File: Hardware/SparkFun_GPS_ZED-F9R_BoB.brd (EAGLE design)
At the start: 43.2 x 50.8 mm, 147 parts, among them J1 U.FL, J3 QWIIC_RIGHT_ANGLE, J4 QWIIC_RIGHT_ANGLE, U1 UBLOX_ZED_F9R, U2 3.3V, U4 HCPL-270L

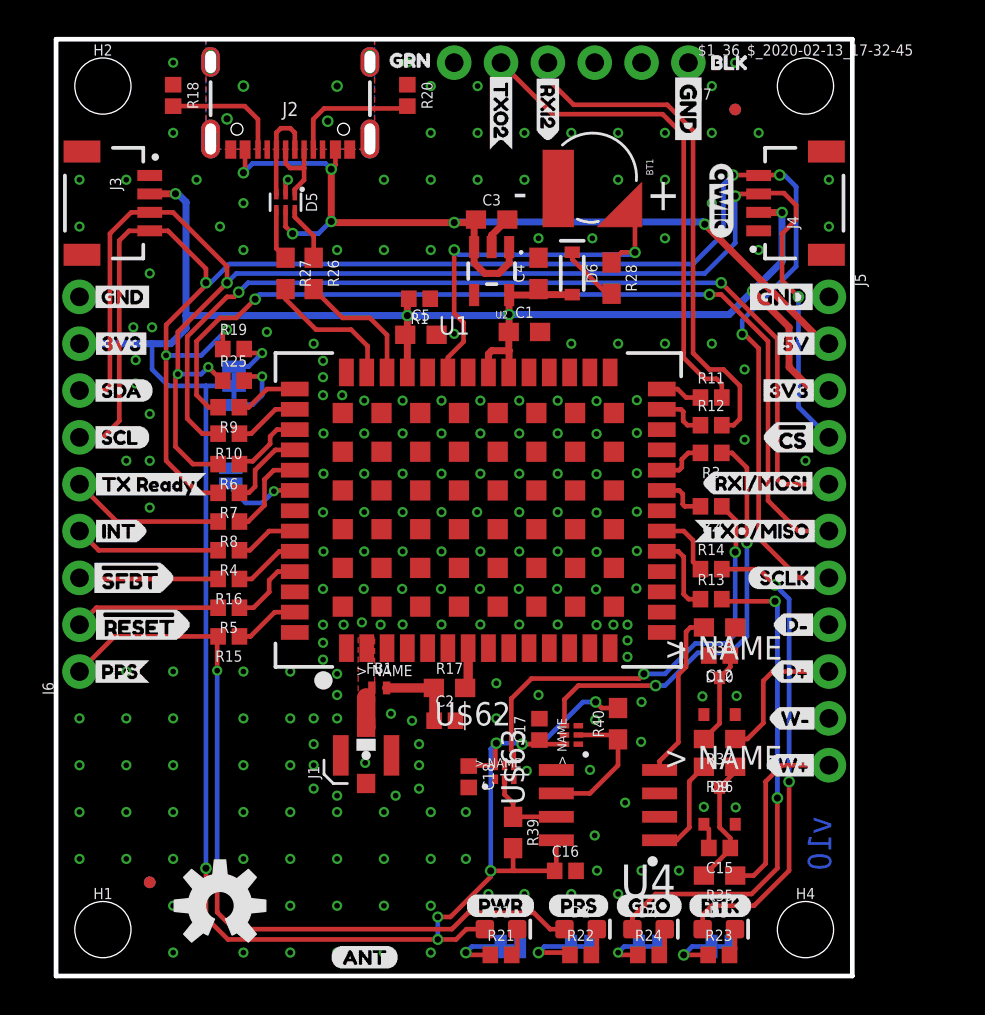
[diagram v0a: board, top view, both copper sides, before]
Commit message: Renumbers parts, updates parts with PROD_IDs that didn't have them before
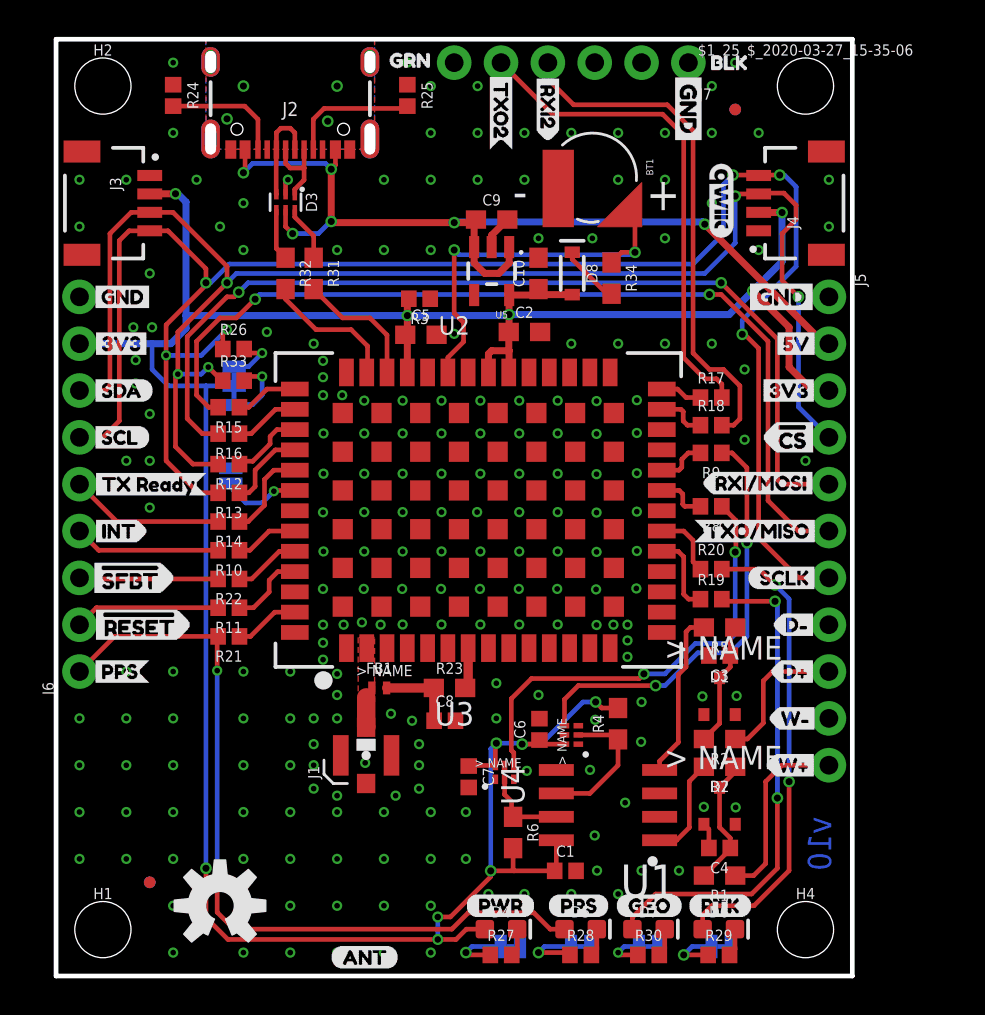
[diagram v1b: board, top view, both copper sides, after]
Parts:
- removed C12, C15: 1nF, SparkFun-Capacitors:0402
- removed C16: 0.1uF, SparkFun-Capacitors:0402
- removed D10, D9: 0.5A/40V/420mV, classified:SOT23_BZX
- removed R35, R37: 3.3k, SparkFun-Resistors:0603
- removed R36, R38: 470, SparkFun-Resistors:0603
- removed R39, R40: 910, classified:0603
- removed U$63: UHS_INVERTER_SCHMITT_TRIGGERSIP6, classified:SIP6
- added C10, C9: 1.0uF, SparkFun-Capacitors:0603
- added C8: 47pF, SparkFun-Capacitors:0402
- added D7: BLUE, SparkFun-LED:LED-0603
- added D8: 0.5A/40V/420mV, SparkFun-DiscreteSemi:SOD-323
- added R29, R30: 1KOHM-0402-1/16W-1%, SparkFun-Resistors:0402
- added R31, R32: 27, SparkFun-Resistors:0603
- added R33: 2.2K, SparkFun-Resistors:0402
- added R34: 3.3k, SparkFun-Resistors:0603
- added U5: 3.3V, SparkFun-IC-Power:SOT23-5
- C1: value 1.0uF -> 0.1uF; device SparkFun-Capacitors:0603 -> SparkFun-Capacitors:0402
- C2: value 47pF -> 1.0uF; device SparkFun-Capacitors:0402 -> SparkFun-Capacitors:0603
- C3, C4: value 1.0uF -> 1nF; device SparkFun-Capacitors:0603 -> SparkFun-Capacitors:0402
- D1: value RED -> 0.5A/40V/420mV; device SparkFun-LED:LED-0603 -> classified:SOT23_BZX
- D2: value BLUE -> 0.5A/40V/420mV; device SparkFun-LED:LED-0603 -> classified:SOT23_BZX
- D3: value BLUE -> PRTR5V0U2F; device SparkFun-LED:LED-0603 -> SparkFun-IC-Power:SOT886
- D4: value BLUE -> RED
- D5: value PRTR5V0U2F -> BLUE; device SparkFun-IC-Power:SOT886 -> SparkFun-LED:LED-0603
- D6: value 0.5A/40V/420mV -> BLUE; device SparkFun-DiscreteSemi:SOD-323 -> SparkFun-LED:LED-0603
- R1: value 100K -> 3.3k; device SparkFun-Resistors:0402 -> SparkFun-Resistors:0603
- R17: device SparkFun-Resistors:0603 -> SparkFun-Resistors:0402
- R18, R20: value 5.1k -> 33
- R19: value 2.2K -> 33
- R2: value 33 -> 3.3k; device SparkFun-Resistors:0402 -> SparkFun-Resistors:0603
- R21, R22: value 1KOHM-0402-1/16W-1% -> 33
- R23: value 1KOHM-0402-1/16W-1% -> 33; device SparkFun-Resistors:0402 -> SparkFun-Resistors:0603
- R24: value 1KOHM-0402-1/16W-1% -> 5.1k
- R25: value 2.2K -> 5.1k
- R26: value 27 -> 2.2K; device SparkFun-Resistors:0603 -> SparkFun-Resistors:0402
- R27: value 27 -> 1KOHM-0402-1/16W-1%; device SparkFun-Resistors:0603 -> SparkFun-Resistors:0402
- R28: value 3.3k -> 1KOHM-0402-1/16W-1%; device SparkFun-Resistors:0603 -> SparkFun-Resistors:0402
- R3: value 33 -> 100K
- R4, R6: value 33 -> 910; device SparkFun-Resistors:0402 -> classified:0603
- R5, R7: value 33 -> 470; device SparkFun-Resistors:0402 -> SparkFun-Resistors:0603
- U1: value UBLOX_ZED_F9R -> HCPL-073L; device classified:UBLOX_ZED_F9R -> classified:SOP_8-PIN
- U2: value 3.3V -> UBLOX_ZED_F9R; device SparkFun-IC-Power:SOT23-5 -> classified:UBLOX_ZED_F9R
- U4: value HCPL-270L -> UHS_INVERTER_SCHMITT_TRIGGERSIP6; device classified:SOP_8-PIN -> classified:SIP6
- moved R24 53.3 mm to (6.35, 47.8), turned to 270 degrees
- moved D3 45.9 mm to (12.4, 42.0), turned to 270 degrees
- moved D5 42.5 mm to (28.4, 2.54), turned to 0 degrees
- moved R27 38.8 mm to (24.1, 1.14), turned to 0 degrees
- moved R28 36.7 mm to (28.4, 1.14), turned to 0 degrees
- moved D6 36.4 mm to (35.9, 2.54), turned to 0 degrees
- moved R1 35.3 mm to (36.0, 5.45)
- moved R18 34.2 mm to (35.5, 29.9), turned to 0 degrees
- moved C4 32.7 mm to (36.0, 6.94), turned to 180 degrees
- moved R20 30.5 mm to (35.5, 22.1), turned to 0 degrees
- moved R7 30.5 mm to (36.0, 11.3)
- moved C1 29.3 mm to (27.6, 5.70)
- moved R19 29.2 mm to (35.5, 20.4)
- moved R11 28.5 mm to (9.37, 20.0), turned to 180 degrees
- moved R22 27.9 mm to (9.37, 21.5), turned to 180 degrees
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- renumbered $1_36_$_2020-02-13_17-32-45 to $1_25_$_2020-03-27_15-35-06, C17 to C6, C18 to C7, U$62 to U3
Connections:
- net !RESET: now also R10.2; no longer R4.2
- net !SAFEBOOT: now also R22.2; no longer R16.2
- net 3.3V: now also C10.1, C2.1, D4.A, D8.A, R3.2, R4.2, R6.2, U1.P8, U2.P33, U2.P34, U2.P38, U4.P6, U5.5; no longer C16.1, C4.1, D1.A, D6.A, R1.2, R39.2, R40.2, U$63.P6, U1.P33, U1.P34, U1.P38, U2.5, U4.P8
- net DIR+: now also R2.1; no longer R37.1
- net DIR_IN: now also R5.2, U1.P4; no longer R38.2, U4.P4
- net DIR_OUT: now also R9.1, U4.P4; no longer R3.1, U$63.P4
- net DIR_SCHMITT: now also R4.1, U1.P6, U4.P2; no longer R40.1, U$63.P2, U4.P6
- net DMINUS: now also R31.2, U2.P39; no longer R26.2, U1.P39
- net DPLUS: now also R32.2, U2.P40; no longer R27.2, U1.P40
- net D_SEL: now also U2.P47; no longer U1.P47
- net GEOF_STAT: now also D7.A, R19.2; no longer D4.A, R13.2
- net GND: now also C10.2, C8.2, C9.2, D1.P1, D2.P1, D3.2, R24.1, R25.1, R3.1, U1.P2, U1.P5, U2.G1, U2.G10, U2.G11, U2.G12, U2.G13, U2.G14, U2.G15, U2.G16, U2.G17, U2.G18, U2.G19, U2.G2, U2.G20, U2.G21, U2.G22, U2.G23, U2.G24, U2.G25, U2.G26, U2.G27, U2.G28, U2.G29, U2.G3, U2.G30, U2.G31, U2.G32, U2.G33, U2.G34, U2.G35, U2.G36, U2.G37, U2.G38, U2.G39, U2.G4, U2.G40, U2.G41, U2.G42, U2.G43, U2.G44, U2.G45, U2.G46, U2.G47, U2.G48, U2.G5, U2.G6, U2.G7, U2.G8, U2.G9, U2.P1, U2.P12, U2.P14, U2.P3, U2.P32, U2.P37, U2.P41, U2.P48, U5.2; no longer C12.2, C15.2, C16.2, D10.P1, D5.2, D9.P1, R1.1, R18.1, R20.1, U$63.P3, U1.G1, U1.G10, U1.G11, U1.G12, U1.G13, U1.G14, U1.G15, U1.G16, U1.G17, U1.G18, U1.G19, U1.G2, U1.G20, U1.G21, U1.G22, U1.G23, U1.G24, U1.G25, U1.G26, U1.G27, U1.G28, U1.G29, U1.G3, U1.G30, U1.G31, U1.G32, U1.G33, U1.G34, U1.G35, U1.G36, U1.G37, U1.G38, U1.G39, U1.G4, U1.G40, U1.G41, U1.G42, U1.G43, U1.G44, U1.G45, U1.G46, U1.G47, U1.G48, U1.G5, U1.G6, U1.G7, U1.G8, U1.G9, U1.P1, U1.P12, U1.P14, U1.P32, U1.P37, U1.P41, U1.P48, U2.2, U4.P2, U4.P5
- net INT: now also R11.2; no longer R5.2
- net N$1: now also R33.2; no longer R25.2
- net N$10: now also D3.4, R32.1; no longer D5.4, R27.1
- net N$11: now also R10.1, U2.P49; no longer R4.1, U1.P49
- net N$12: now also R11.1, U2.P51; no longer R5.1, U1.P51
- net N$14: now also R24.2; no longer R18.2
- net N$15: now also R25.2; no longer R20.2
- net N$16: now also R12.1, U2.P44; no longer R6.1, U1.P44
- net N$17: now also R13.1, U2.P45; no longer R7.1, U1.P45
- net N$18: now also R14.1, U2.P46; no longer R8.1, U1.P46
- net N$19: now also R15.1, U2.P42; no longer R9.1, U1.P42
- net N$2: now also D8.C, R34.2; no longer D6.C, R28.2
- net N$20: now also R16.1, U2.P43; no longer R10.1, U1.P43
- net N$21: now also R17.1, U2.P27; no longer R11.1, U1.P27
- net N$22: now also R29.1; no longer R23.1
- net N$23: now also R28.1; no longer R22.1
- net N$24: now also D5.C, R28.2; no longer D2.C, R22.2
- net N$25: now also D6.C, R29.2; no longer D3.C, R23.2
- net N$26: now also R18.1, U2.P26; no longer R12.1, U1.P26
- net N$27: now also R19.1, U2.P19; no longer R13.1, U1.P19
- net N$28: now also R20.1, U2.P20; no longer R14.1, U1.P20
- net N$29: now also R21.1, U2.P53; no longer R15.1, U1.P53
- net N$3: now also R26.2; no longer R19.2
- net N$30: now also R22.1, U2.P50; no longer R16.1, U1.P50
- net N$31: now also R8.2, U2.P22; no longer R2.2, U1.P22
- net N$32: now also R9.2, U2.P23; no longer R3.2, U1.P23
- net N$33: now also R30.1; no longer R24.1
- net N$34: now also D7.C, R30.2; no longer D4.C, R24.2
- net N$35: now also C4.1, D2.P3, R1.2, R7.1; no longer C15.1, D9.P3, R35.2, R36.1
- net N$37: now also C3.1, D1.P3, R2.2, R5.1; no longer C12.1, D10.P3, R37.2, R38.1
- net N$4: now also D4.C, R27.2; no longer D1.C, R21.2
- net N$5: now also C8.1, R23.1; no longer C2.1, R17.1
- net N$6: now also D3.3; no longer D5.3
- net N$7: now also D3.1; no longer D5.1
- net N$8: now also R27.1; no longer R21.1
- net N$9: now also D3.6, R31.1; no longer D5.6, R26.1
- net PPS: now also D5.A, R21.2; no longer D2.A, R15.2
- net RF_IN: now also U2.P2; no longer U1.P2
- net RTK_STAT: now also D6.A, R20.2; no longer D3.A, R14.2
- net RXI/MOSI: now also R16.2; no longer R10.2
- net RXI2: now also R18.2; no longer R12.2
- net SCL/CLK: now also R13.2, R26.1; no longer R19.1, R7.2
- net SDA/!CS: now also R12.2, R33.1; no longer R25.1, R6.2
- net TXO/MISO: now also R15.2; no longer R9.2
- net TXO2: now also R17.2; no longer R11.2
- net TX_READY: now also R14.2; no longer R8.2
- net VIN: now also C9.1, D3.5, U5.1, U5.3; no longer C3.1, D5.5, U2.1, U2.3
- net V_BATT: now also R34.1, U2.P36; no longer R28.1, U1.P36
- net V_RF: now also R23.2, U2.P7; no longer R17.2, U1.P7
- net WT+: now also R1.1; no longer R35.1
- net WT_IN: now also R7.2, U1.P1; no longer R36.2, U4.P1
- net WT_OUT: now also R8.1; no longer R2.1
- net WT_SCHMITT: now also R6.1, U1.P7; no longer R39.1, U4.P7

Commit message: Updates silk, fixes RF trace, moves some traces for better clearance
* Fixes various small design issues
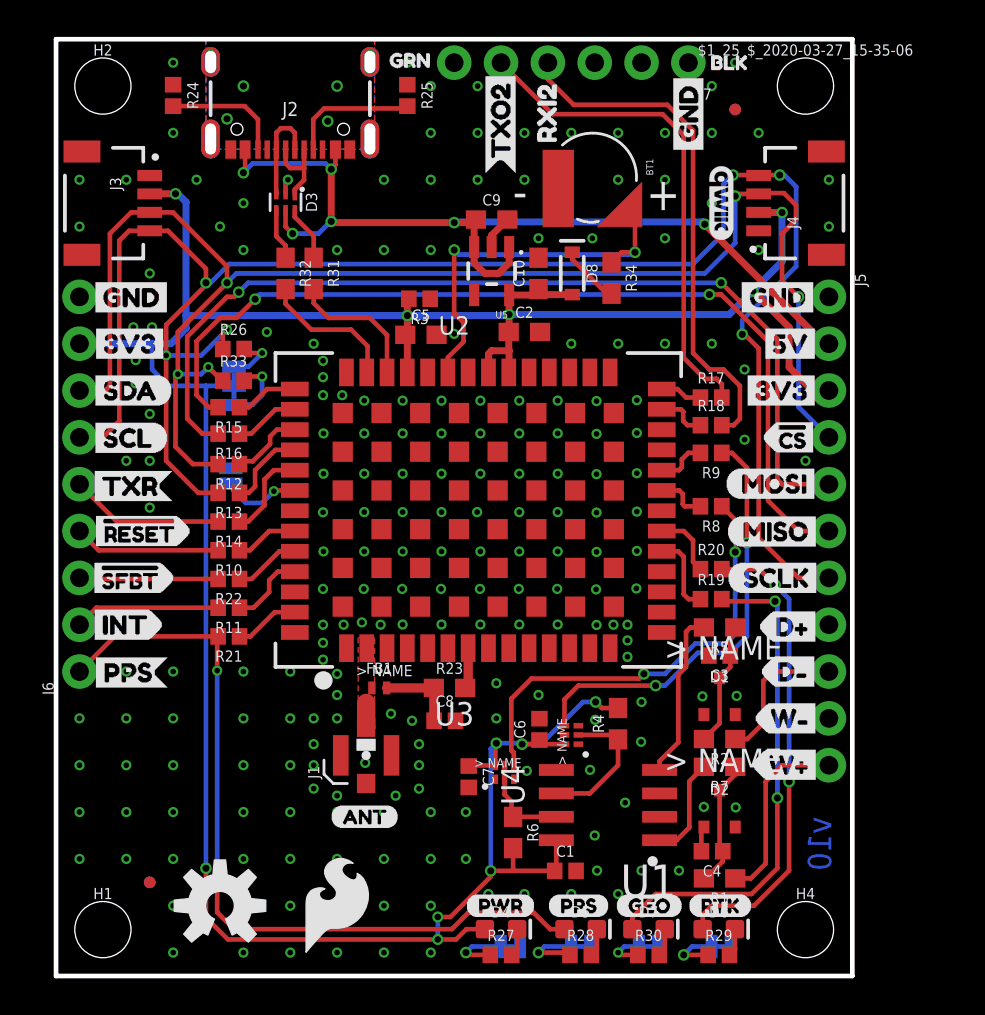
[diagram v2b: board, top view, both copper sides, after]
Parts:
- removed U$19: (no value), I2C Buzzard Labels Small:3V32
- removed U$20: (no value), Labels:GND-03
- removed U$25: (no value), rx lables:TXO21
- removed U$32: (no value), WT_dir_small:W#2
- removed U$50: (no value), WT_dir_small:W#3
- removed U$57: (no value), wat-for-reals:SCLK2
- added U$62: (no value), SparkFun-Aesthetics:SFE_LOGO_FLAME_.2
- added U$66: (no value), Labels:MISO-(]-04
- added U$67: (no value), Labels:SCL-[)
- added U$68: (no value), Labels:SDA-[)
- added U$69: (no value), Labels:MOSI-(]-04
- added U$70: (no value), Labels:3V3-04
- added U$71: (no value), Labels:GND-04
- U$1: device ALL labels:INT2 -> Labels:3V3-04
- U$10: device WT_dir_small:D#0 -> wt_dir:W#3
- U$11: device scl:SCL0 -> Labels:5V
- U$12: device I2C Buzzard Labels Small:SDA1 -> ALL_LABELS:INT1
- U$13: device WT_dir_small:D#1 -> ALL_LABELS:PPS4
- U$14: device rx lables:RXI22 -> txr_rxi:RXI22
- U$15: device ALL labels:TXO#MISO6 -> Labels:GND-04
- U$16: device ALL labels:TX_READY0 -> moar:TXO21
- U$17: device Labels:GND-03 -> txr_rxi:SCLK1
- U$18: device 5V:5V0 -> txr_rxi:TXR0
- U$2: device ALL labels:PPS4 -> Labels:GND-04
- U$3: device I2C Buzzard Labels Small:3V32 -> wt_dir:D#0
- U$6: device I2C Buzzard Labels Small:GND3 -> wt_dir:D#1
- U$9: device ALL labels:RXI#MOSI5 -> wt_dir:W#2
- moved U$6 41.7 mm to (38.2, 16.5)
- moved U$2 40.4 mm to (36.7, 36.8)
- moved U$3 39.4 mm to (38.1, 18.9)
- moved U$18 38.0 mm to (1.57, 26.6)
- moved U$13 37.3 mm to (1.68, 16.5)
- moved U$11 36.5 mm to (37.9, 34.3)
- moved U$1 36.0 mm to (37.0, 31.8)
- moved U$16 27.9 mm to (24.1, 43.4), turned to 90 degrees
- moved U$15 20.2 mm to (34.3, 44.3), turned to 90 degrees
- moved U$9 15.5 mm to (37.7, 11.5)
- moved U$17 15.3 mm to (36.3, 21.6)
- moved U$12 12.7 mm to (1.57, 19.1)
- moved U$49 7.62 mm to (14.9, 8.64)
- moved U$24 5.08 mm to (5.84, 19.1)
- moved U$44 5.08 mm to (1.52, 24.1)
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- renumbered JP1 to PWR, JP2 to PPS, JP3 to RTK, JP4 to GEOF

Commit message: Removes 0402 33 Ohm resistors in place of 33Ohm resistor bank
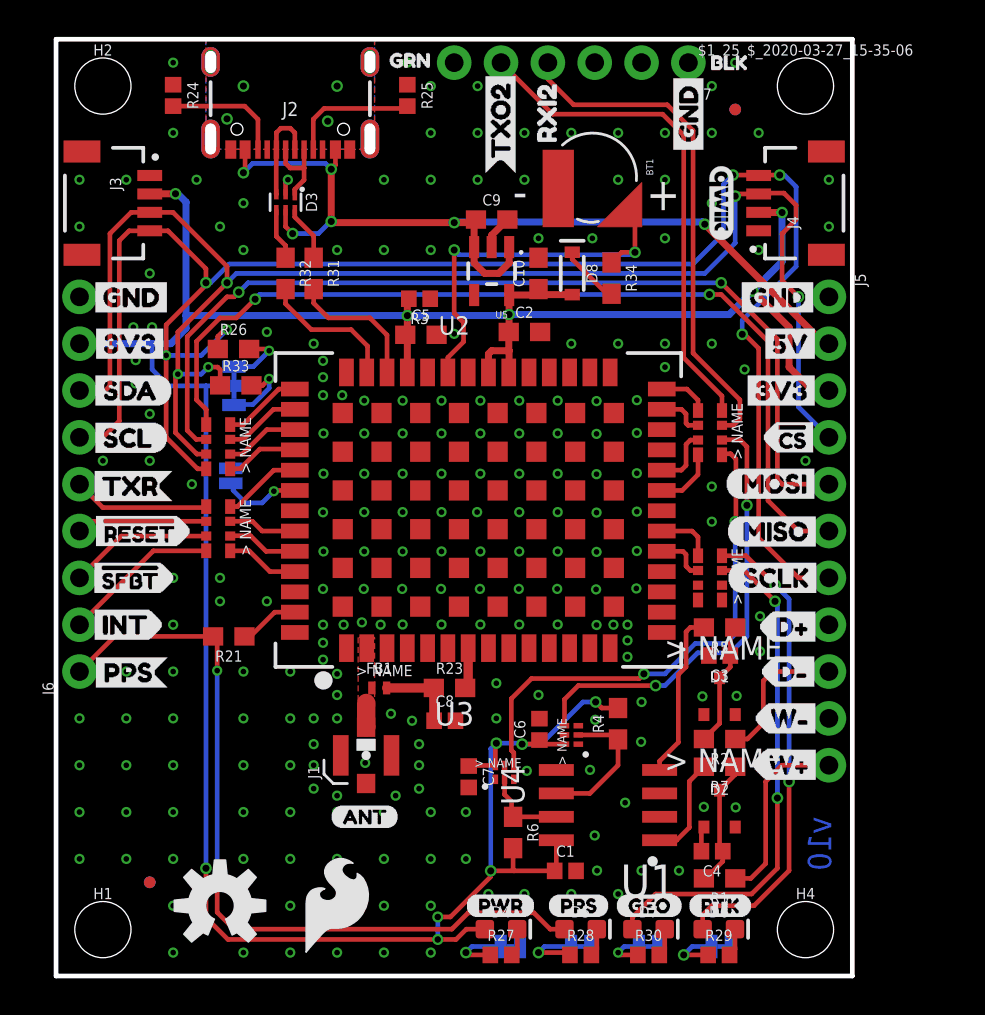
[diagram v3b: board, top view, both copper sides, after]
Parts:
- removed R12, R14, R15, R16, R17, R18, R19, R20, R22, R9: 33, SparkFun-Resistors:0402
- R10, R11, R13, R8: device SparkFun-Resistors:0402 -> SparkFun-Resistors:1206_RA
- R21: device SparkFun-Resistors:0402 -> SparkFun-Resistors:0603
- R26, R33: value 2.2K -> 2.2k; device SparkFun-Resistors:0402 -> SparkFun-Resistors:0603
- moved R13 26.3 mm to (35.4, 29.5), turned to 270 degrees
- moved R10 5.65 mm to (8.76, 28.7), turned to 270 degrees
- moved R11 4.33 mm to (8.76, 24.3), turned to 270 degrees
- moved R8 3.88 mm to (35.4, 21.6), turned to 270 degrees
- moved R33 0.28 mm to (9.75, 32.0)
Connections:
- net !RESET: now also R11.P2; no longer R10.2
- net !SAFEBOOT: now also R11.P3; no longer R22.2
- net DIR_OUT: now also R13.P6; no longer R9.1
- net GEOF_STAT: now also R8.P7; no longer R19.2
- net INT: now also R11.P4; no longer R11.2
- net N$11: now also R11.P7; no longer R10.1
- net N$12: now also R11.P5; no longer R11.1
- net N$16: now also R10.P6; no longer R12.1
- net N$17: now also R10.P5; no longer R13.1
- net N$18: now also R11.P8; no longer R14.1
- net N$19: now also R10.P8; no longer R15.1
- net N$20: now also R10.P7; no longer R16.1
- net N$21: now also R13.P1; no longer R17.1
- net N$26: now also R13.P2; no longer R18.1
- net N$27: now also R8.P2; no longer R19.1
- net N$28: now also R8.P1; no longer R20.1
- net N$30: now also R11.P6; no longer R22.1
- net N$31: now also R13.P4; no longer R8.2
- net N$32: now also R13.P3; no longer R9.2
- net RTK_STAT: now also R8.P8; no longer R20.2
- net RXI/MOSI: now also R10.P2; no longer R16.2
- net RXI2: now also R13.P7; no longer R18.2
- net SCL/CLK: now also R10.P4; no longer R13.2
- net SDA/!CS: now also R10.P3; no longer R12.2
- net TXO/MISO: now also R10.P1; no longer R15.2
- net TXO2: now also R13.P8; no longer R17.2
- net TX_READY: now also R11.P1; no longer R14.2
- net WT_OUT: now also R13.P5; no longer R8.1
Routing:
- net WT_OUT: track 24.5 -> 27.7 mm
- net SCL/CLK: track 99.6 -> 97.9 mm
- net N$27: track 4.36 -> 2.77 mm
- net DIR_OUT: track 23.6 -> 24.5 mm
- net TX_READY: track 8.36 -> 7.42 mm
- net N$19: track 3.41 -> 4.30 mm
- net !RESET: track 7.95 -> 7.09 mm
- net SDA/!CS: track 83.2 -> 82.3 mm
- net N$18: track 4.97 -> 4.32 mm
- net GEOF_STAT: track 27.1 -> 27.7 mm
- net INT: track 7.90 -> 8.53 mm
- net N$20: track 3.55 -> 4.18 mm
- net N$31: track 2.78 -> 3.39 mm
- net N$32: track 2.74 -> 3.31 mm
- net N$17: track 4.49 -> 3.97 mm
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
